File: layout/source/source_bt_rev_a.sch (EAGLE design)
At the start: 17 parts, among them IC1 LP2985-SOT23-5, IC2 IC_USBLC6-2, IC3 HM-10

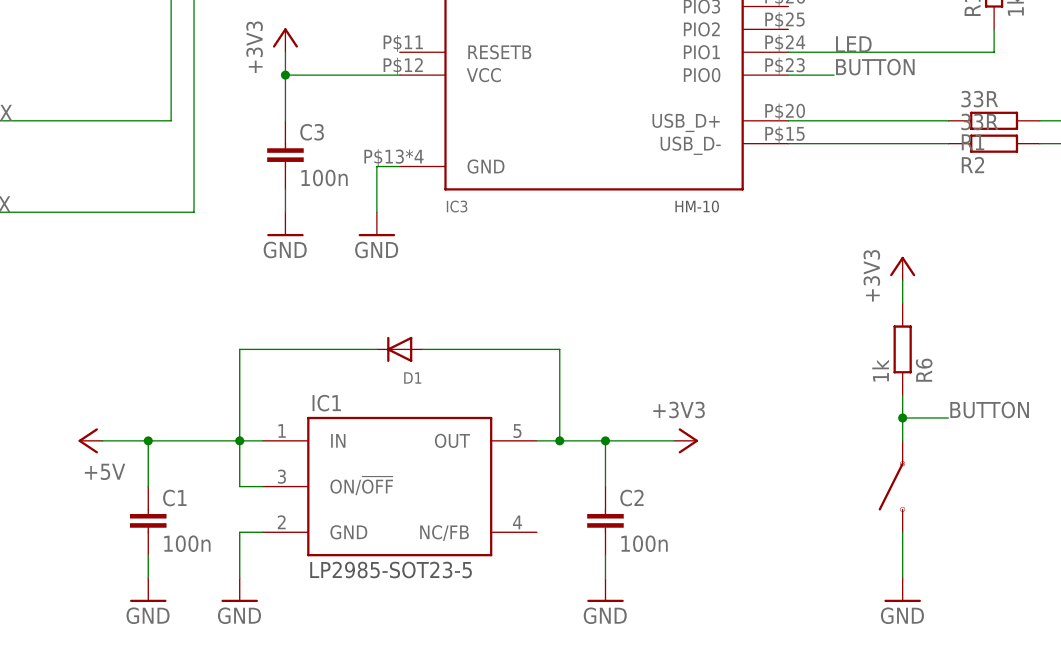
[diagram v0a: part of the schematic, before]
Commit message: Changed structure, added HM-11
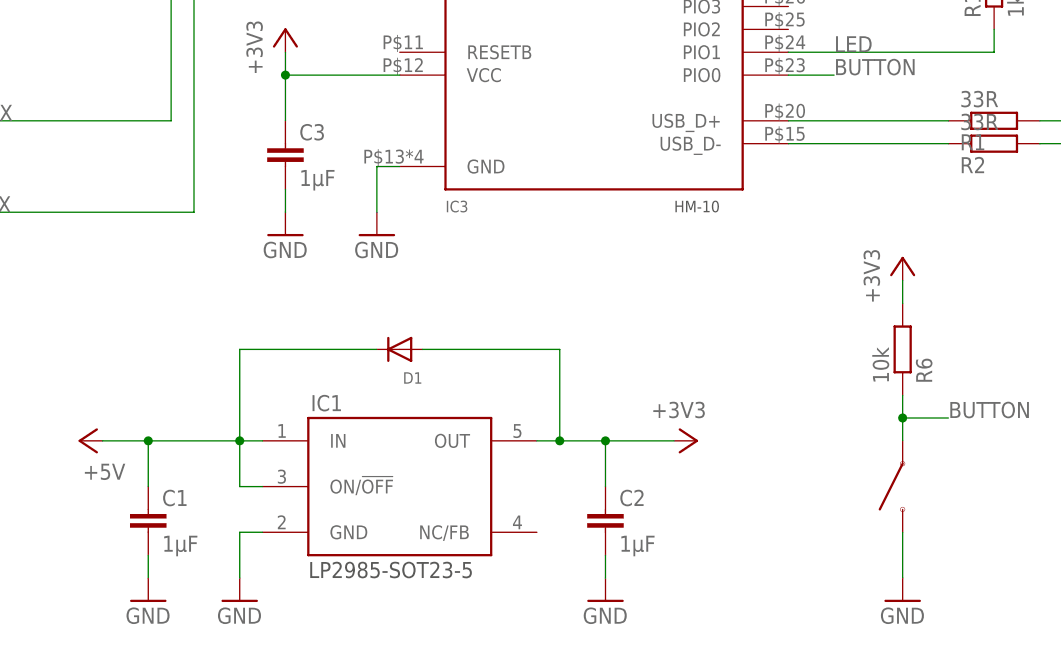
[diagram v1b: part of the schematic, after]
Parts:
- C1, C2, C3: value 100n -> 1µF
- R6: value 1k -> 10k
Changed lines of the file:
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@@
 <part name="IC2" library="dp_devices" deviceset="IC_USBLC6-2" device=""/>
 <part name="TRS1" library="con-trs" deviceset="PJ-3504" device=""/>
-<part name="C3" library="rcl" deviceset="C-EU" device="C0603" value="100n"/>
+<part name="C3" library="rcl" deviceset="C-EU" device="C0603" value="1µF"/>
 <part name="R3" library="rcl" deviceset="R-EU_" device="R0603" value="33R"/>
 <part name="R4" library="rcl" deviceset="R-EU_" device="R0603" value="33R"/>
@@
 <part name="D1" library="microbuilder" deviceset="DIODE" device="SOD-323"/>
 <part name="GND5" library="supply1" deviceset="GND" device=""/>
-<part name="C1" library="rcl" deviceset="C-EU" device="C0603" value="100n"/>
-<part name="C2" library="rcl" deviceset="C-EU" device="C0603" value="100n"/>
+<part name="C1" library="rcl" deviceset="C-EU" device="C0603" value="1µF"/>
+<part name="C2" library="rcl" deviceset="C-EU" device="C0603" value="1µF"/>
 <part name="P+1" library="supply1" deviceset="+5V" device=""/>
 <part name="GND6" library="supply1" deviceset="GND" device=""/>
 <part name="GND7" library="supply1" deviceset="GND" device=""/>
 <part name="P+2" library="supply1" deviceset="+5V" device=""/>
-<part name="R6" library="rcl" deviceset="R-EU_" device="R0603" value="1k"/>
+<part name="R6" library="rcl" deviceset="R-EU_" device="R0603" value="10k"/>
 <part name="+3V3" library="supply1" deviceset="+3V3" device=""/>
 </parts>
